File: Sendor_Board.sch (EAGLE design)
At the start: 36 parts, among them Q1 8.000Mhz, U1 PIC32MX795F512H-80I/PT, U2 SHT25, U3 MPL115A2, U4 MRF24J40MA, X1 MINI-USB-SHIELD-UX60A-MB-5ST

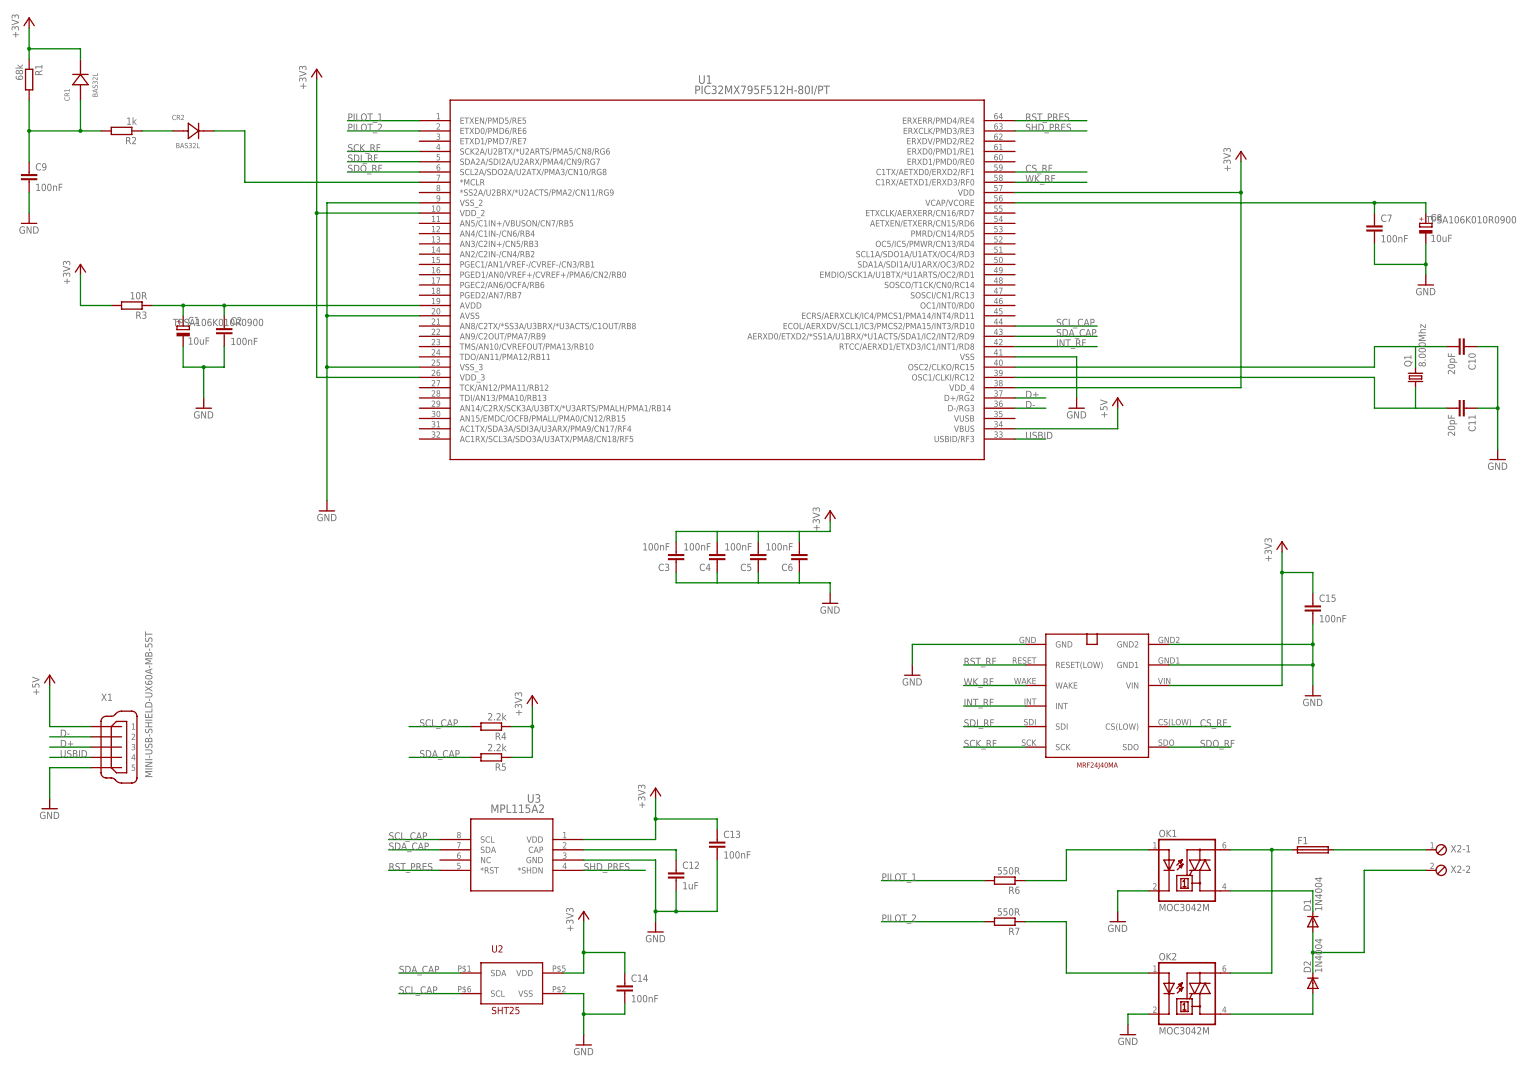
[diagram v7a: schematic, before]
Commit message: Change all presentation an add a frame
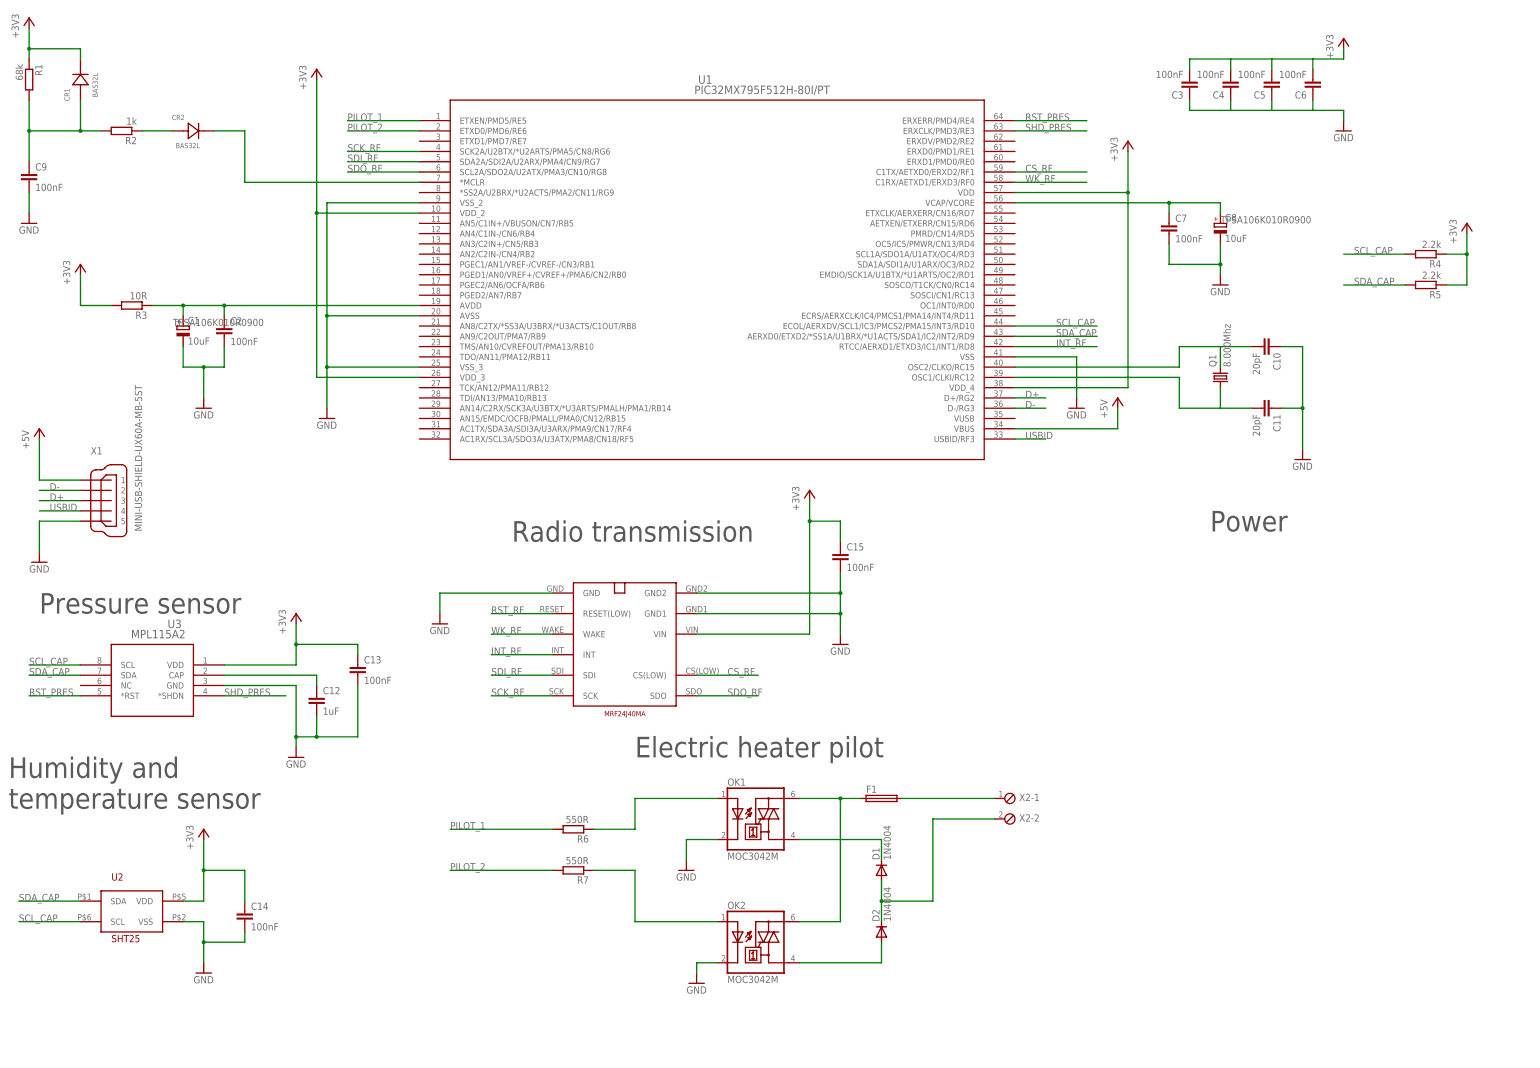
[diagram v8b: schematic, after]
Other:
- note added: "Electric heater pilot"
- note added: "Humidity and temperature sensor"
- note added: "Power"
- note added: "Pressure sensor"
- note added: "Radio transmission"
- moved on the sheet: C10, C11, C12, C13, C14, C15, C3, C4, C5, C6, C7, C8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
